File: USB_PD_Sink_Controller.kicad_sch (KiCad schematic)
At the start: 25 parts, among them J1 USB_C_Receptacle_PowerOnly_6P, J2 Barrel_Jack, J3 Conn_01x15_Socket, J4 Conn_01x15_Socket, U1 STUSB4500QTR, U2 STL6P3LLH6, U3 STL6P3LLH6, U4 LM2931-5.0_SO8

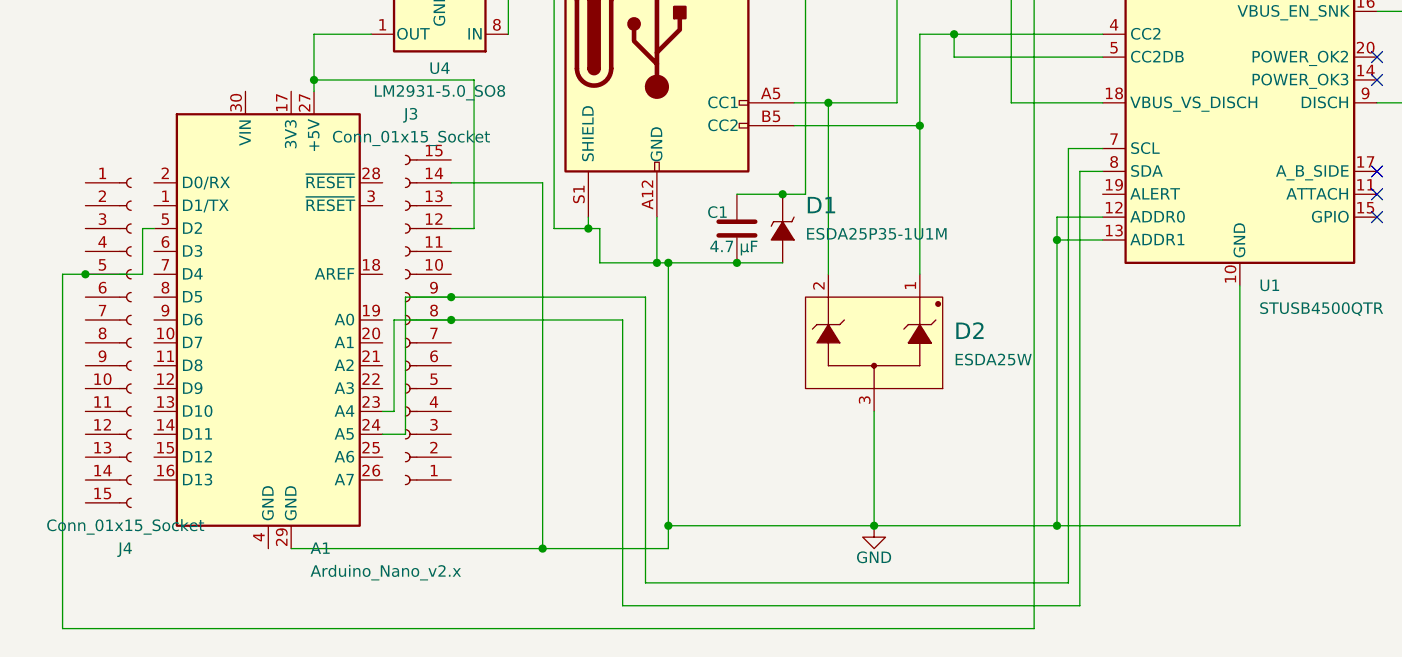
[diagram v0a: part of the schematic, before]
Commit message: Added Pullup resistors and alert pin
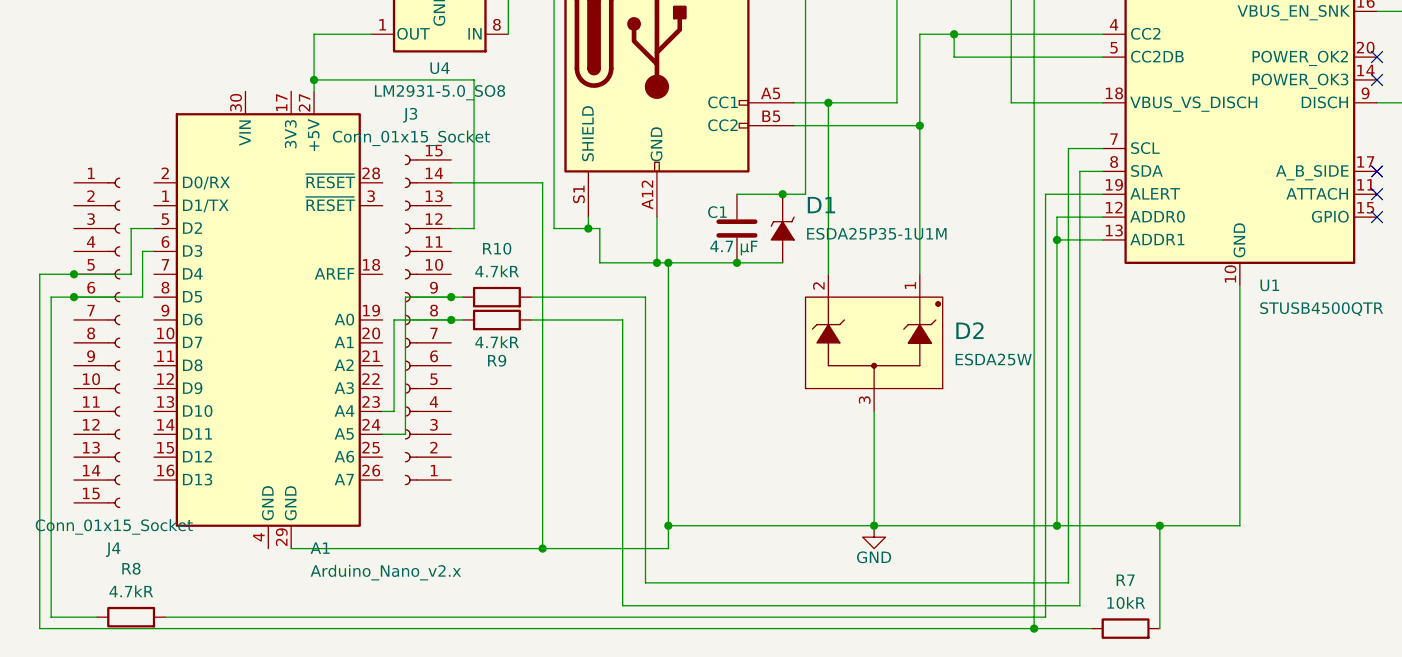
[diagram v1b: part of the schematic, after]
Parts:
- added R10, R8, R9: 4.7kR, Resistor_SMD:R_0603_1608Metric_Pad0.98x0.95mm_HandSolder, symbol Device:R
- added R7: 10kR, Resistor_SMD:R_0603_1608Metric_Pad0.98x0.95mm_HandSolder, symbol Device:R
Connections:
- net GND: now also R7.2
- net at A1.5 (D2), J4.5 (Pin_5), U1.6 (RESET): now also R7.1
- net at J4.6 (Pin_6): now also A1.6 (D3), R8.1
- net at U1.19 (ALERT): now also R8.2
- net at A1.24 (A5), J3.9 (Pin_9): now also R10.1; no longer U1.7 (SCL)
- net at A1.23 (A4), J3.8 (Pin_8): now also R9.1; no longer U1.8 (SDA)
- new net: R10.2, U1.7 (SCL)
- new net: R9.2, U1.8 (SDA)
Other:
- moved on the sheet: J4

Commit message: Added capacitor to linear voltage regulator
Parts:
- added C7: 100μF, Capacitor_SMD:C_0603_1608Metric_Pad1.08x0.95mm_HandSolder, symbol Device:C
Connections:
- net GND: now also C7.1
- net at A1.27 (+5V), J3.12 (Pin_12), U4.1 (OUT): now also C7.2
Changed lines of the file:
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@@
+	)
+	(junction
+		(at 45.72 86.36)
+		(diameter 0)
+		(color 0 0 0 0)
 	)
 	(junction
@@
 	)
 	(junction
+		(at 59.69 78.74)
+		(diameter 0)
+		(color 0 0 0 0)
+	)
+	(junction
 		(at 45.72 91.44)
 		(diameter 0)
@@
 		(pts
 			(xy 254 22.86) (xy 254 35.56)
+		)
+		(stroke
+			(width 0)
+			(type default)
+		)
+	)
+	(wire
+		(pts
+			(xy 45.72 78.74) (xy 59.69 78.74)
 		)
 		(stroke
@@
 					(unit 1)
 				)
+			)
+		)
+	)
+	(symbol
+		(lib_id "Device:C")
+		(at 45.72 82.55 0)
+		(unit 1)
+		(exclude_from_sim no)
+		(in_bom yes)
+		(on_board yes)
+		(dnp no)
+		(property "Reference" "C7"
+			(at 49.53 81.2799 0)
+			(effects
+				(font
+					(size 1.27 1.27)
+				)
+				(justify left)
+			)
+		)
+		(property "Value" "100μF"
+			(at 48.26 83.566 0)
+			(effects
+				(font
+					(size 1.27 1.27)
+				)
+				(justify left)
+			)
+		)
+		(property "Footprint" "Capacitor_SMD:C_0603_1608Metric_Pad1.08x0.95mm_HandSolder"
+			(at 46.6852 86.36 0)
+			(effects
+				(font
+					(size 1.27 1.27)
+				)
+				(hide yes)
+			)
+		)
+		(property "Datasheet" "~"
+			(at 45.72 82.55 0)
+			(effects
+				(font
+					(size 1.27 1.27)
+				)
+				(hide yes)
+			)
+		)
+		(property "Description" "Unpolarized capacitor"
+			(at 45.72 82.55 0)
+			(effects
+				(font
+					(size 1.27 1.27)
+				)
+				(hide yes)
+			)
+		)
+		(pin "1"
+		)
+		(pin "2"
+		)
+		(instances
+			(project "USB_PD_Sink_Controller"
+				(path "/402bd669-350c-4e2f-bbb5-342e789ed039"
+					(reference "C7")
+					(unit 1)
+				)

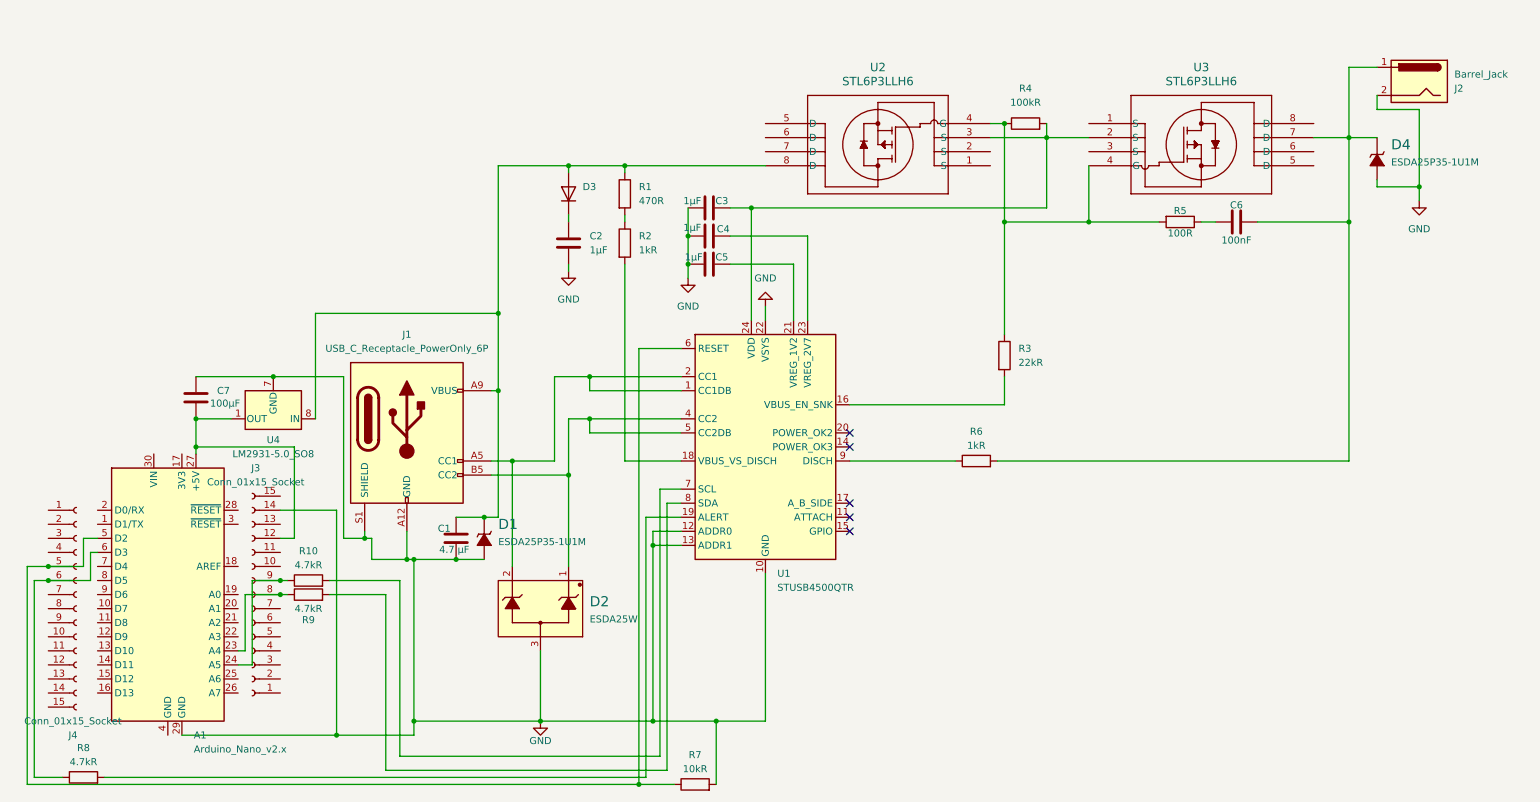
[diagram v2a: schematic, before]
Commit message: Revamped the PCB design
Made many of the traces thicker. Changed from a barrel jack to a JST connector. Made the schematic pretty. Made the Arduino Nano directly soldered onto the board. Etc.
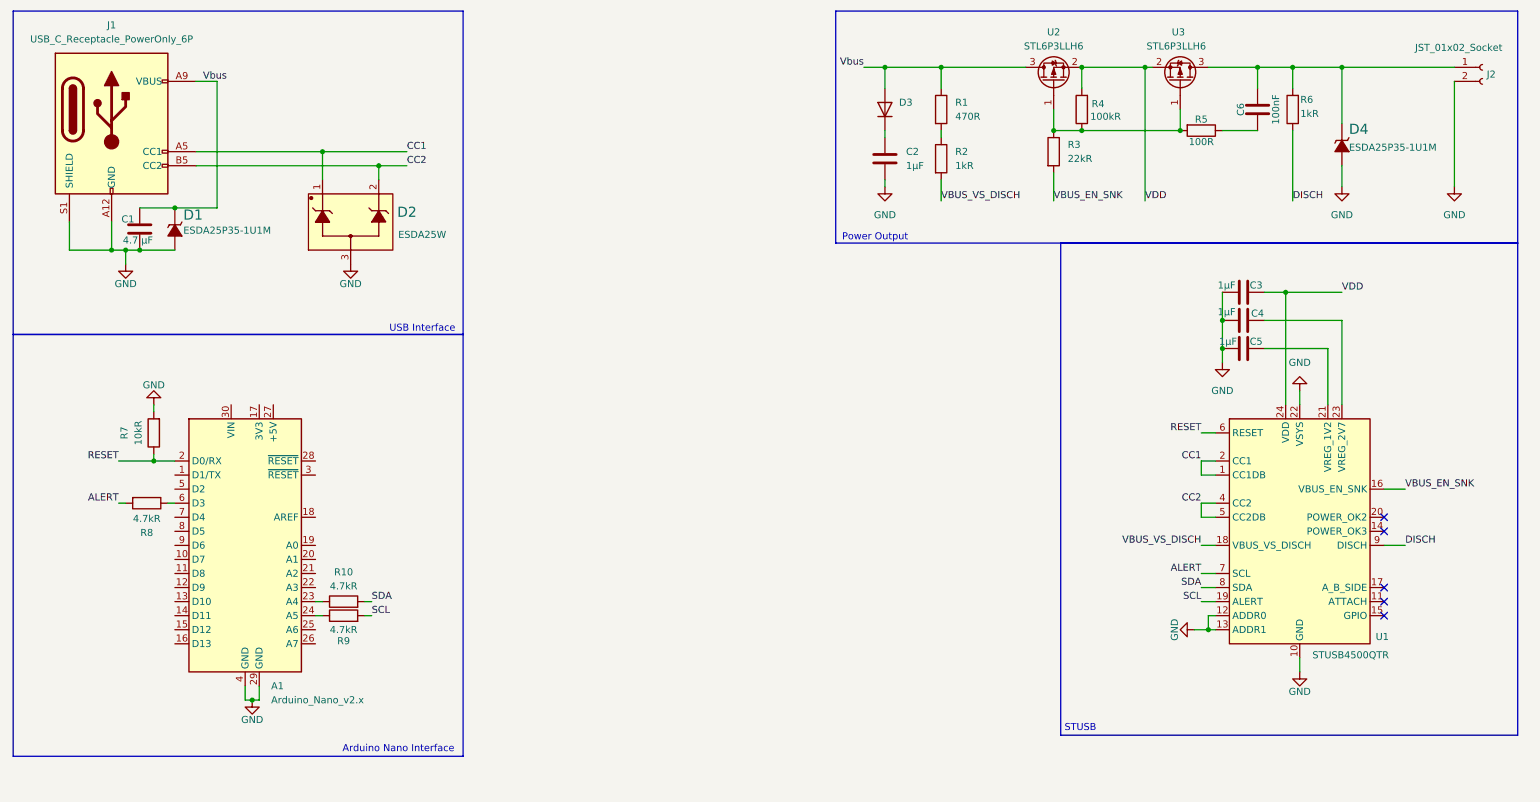
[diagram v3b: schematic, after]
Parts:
- removed C7: 100μF, Capacitor_SMD:C_0603_1608Metric_Pad1.08x0.95mm_HandSolder, symbol Device:C
- removed J2: Barrel_Jack, Connector_BarrelJack:BarrelJack_CUI_PJ-102AH_Horizontal, symbol Connector:Barrel_Jack
- removed J3, J4: Conn_01x15_Socket, Connector_PinSocket_2.54mm:PinSocket_1x15_P2.54mm_Vertical, symbol Connector:Conn_01x15_Socket
- removed U2, U3: STL6P3LLH6, STL6P3LLH6:POWERFLAT_3P3X3P3_STM, symbol STL6P3LLH6:STL6P3LLH6
- removed U4: LM2931-5.0_SO8, Package_SO:SOIC-8_3.9x4.9mm_P1.27mm, symbol Regulator_Linear:LM2931-5.0_SO8
- added J2: JST_01x02_Socket, Connector_JST:JST_XH_B2B-XH-AM_1x02_P2.50mm_Vertical, symbol Connector:Conn_01x02_Socket
- added U2, U3: STL6P3LLH6, STL6P3LLH6:POWERFLAT_3P3X3P3_STM2, symbol Transistor_FET:AO3401A
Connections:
- net GND: now also A1.4 (GND), J2.2 (Pin_2)
- net Vbus: now reaches C1.1, D1.1 (K), D3.2 (A), J1.A9 (VBUS), J1.B9 (VBUS), R1.1
- net Vbus: now also U2.3 (D)
- net VDD: now reaches C3.2, R4.2, U1.24 (VDD)
- net VDD: now also U2.2 (S), U3.2 (S)
- net DISCH: now reaches R6.1, U1.9 (DISCH)
- net at C6.2, D4.1 (K), R6.2: now also J2.1 (Pin_1), U3.3 (D)
- net RESET: now reaches R7.1, U1.6 (RESET)
- net RESET: now also A1.2 (D0/RX); no longer A1.5 (D2)
- net ALERT: now reaches R8.2
- net ALERT: now also U1.7 (SCL); no longer U1.19 (ALERT)
- net CC1: now reaches J1.A5 (CC1), U1.1 (CC1DB), U1.2 (CC1)
- net CC1: now also D2.1; no longer D2.2
- net VBUS_EN_SNK: now reaches R3.2, U1.16 (VBUS_EN_SNK)
- net VBUS_VS_DISCH: now reaches R2.2, U1.18 (VBUS_VS_DISCH)
- net CC2: now reaches J1.B5 (CC2), U1.4 (CC2), U1.5 (CC2DB)
- net CC2: now also D2.2; no longer D2.1
- net SDA: now reaches R10.2
- net SDA: now also U1.8 (SDA); no longer U1.7 (SCL)
- net SCL: now reaches R9.2
- net SCL: now also U1.19 (ALERT); no longer U1.8 (SDA)
- net at R3.1, R4.1, R5.2: now also U2.1 (G), U3.1 (G)
- net at A1.23 (A4): now also R10.1; no longer R9.1
- net at A1.24 (A5): now also R9.1; no longer R10.1
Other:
- note added: "Arduino Nano Interface"
- note added: "Power Output"
- note added: "STUSB"
- note added: "USB Interface"
- moved on the sheet: A1, C1, C2, C3, C4, C5, C6, D1, D2, D3, D4, J1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
